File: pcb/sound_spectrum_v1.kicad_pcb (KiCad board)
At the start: 4 copper layers, 85.6 x 54 mm, 31 parts, among them J1 SWD_CONN, J2 Conn_02x10_Counter_Clockwise, P1 USB_C_Plug_USB2.0, SW2 SW_DPST_x2, U1 STM32G473CBTx, U2 AP2112K-3.3, U3 USBLC6-2SC6

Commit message: chore: further tracing
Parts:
- C12, C13, MK1-L1, MK1-R1: moved to B.Cu
- moved MK1-R1 60.6 mm to (125.8, 116.1), turned to 180 degrees
- moved J1 49.3 mm to (135.5, 72.7), turned to -90 degrees
- moved C13 43.1 mm to (123.5, 113.0), turned to 180 degrees
- moved MK1-L1 42.3 mm to (193.5, 116.0), turned to 180 degrees
- moved C14 40.6 mm to (126.2, 74.0), turned to 90 degrees
- moved U3 38.8 mm to (159.1, 79.6), turned to 90 degrees
- moved C12 38.4 mm to (191.2, 112.8), turned to 180 degrees
- moved SW2 38.4 mm to (141.8, 72.8)
- moved R4 36.1 mm to (170.2, 74.5), turned to 90 degrees
- moved FB1 33.9 mm to (167.0, 88.0)
- moved U2 29.2 mm to (167.7, 82.1), turned to -90 degrees
- moved R3 27.4 mm to (162.5, 79.5), turned to -90 degrees
- moved R6 26.6 mm to (146.0, 95.0), turned to 90 degrees
- moved D2 23.0 mm to (167.5, 74.5), turned to -90 degrees
- moved R5 22.9 mm to (148.2, 95.0), turned to 90 degrees
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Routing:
- net +3.3V: track 0.00 -> 112.2 mm
- net SWO: track 0.00 -> 31.6 mm
- net SWCLK: track 0.00 -> 28.5 mm
- net SWDIO: track 0.00 -> 28.5 mm
- net NRST: track 0.00 -> 27.0 mm
- net VBUS: track 0.00 -> 26.6 mm
- net USB_DP: track 0.00 -> 13.4 mm
- net USB_DM: track 0.00 -> 9.27 mm
- net I2C_SDA: track 0.00 -> 8.96 mm, vias 0 -> 2
- net +5V: track 0.00 -> 5.08 mm
- net BOOT0: track 0.00 -> 3.94 mm
- net Net-(P1-CC): track 0.00 -> 3.94 mm
- net USB_DM_EXT: track 0.00 -> 3.63 mm, vias 0 -> 1
- net USB_DP_EXT: track 0.00 -> 3.01 mm
- net Net-(D2-A): track 0.00 -> 2.76 mm
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- added copper zone on In1.Cu, net GND
- added copper zone on In2.Cu, net GND

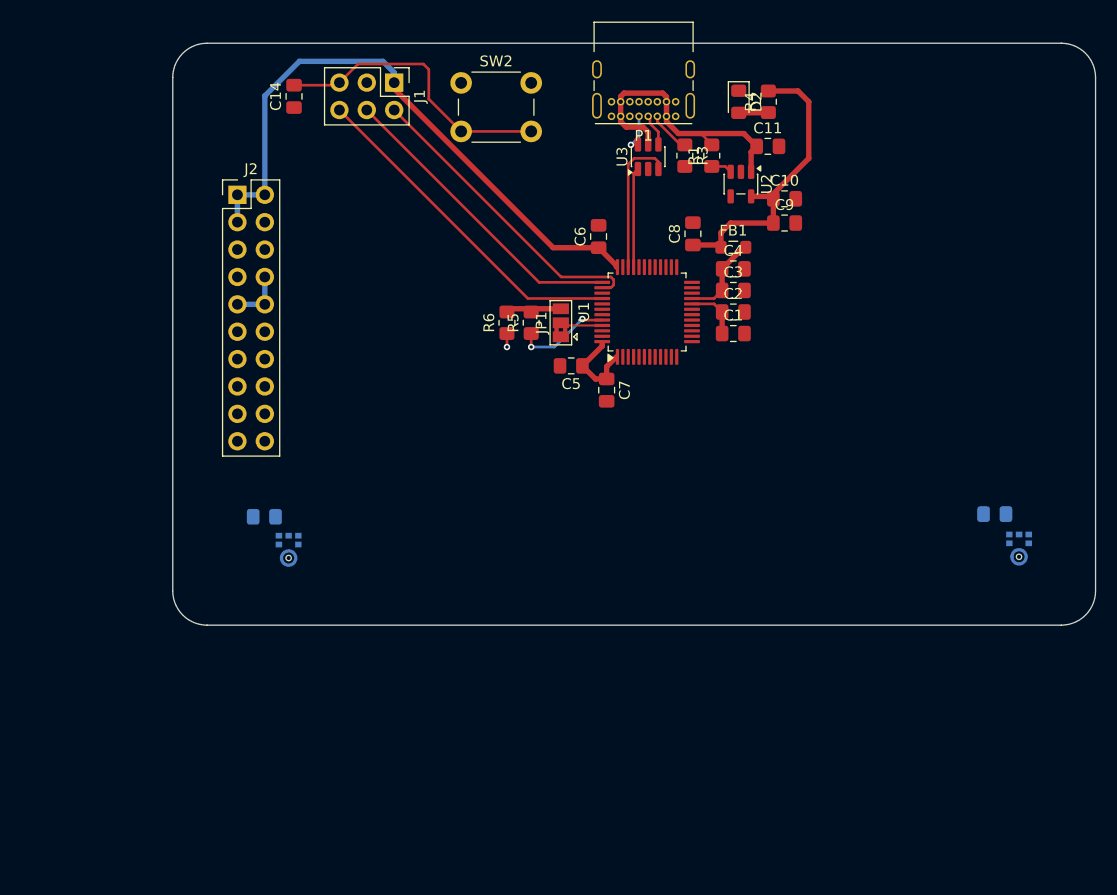
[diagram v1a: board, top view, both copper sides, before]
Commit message: fix: replace ics-43434 with ics-43432 due to part shortage
feat: make connections to all parts
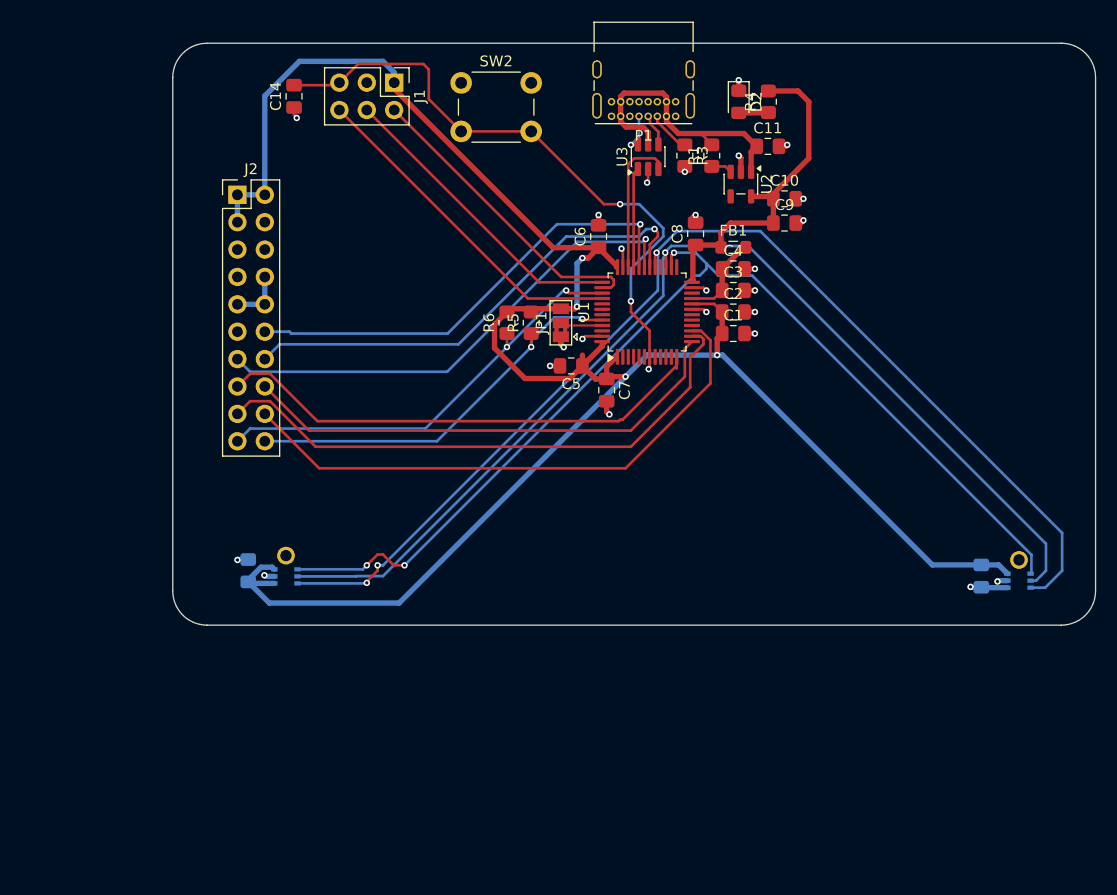
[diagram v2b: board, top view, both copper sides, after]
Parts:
- removed MK1-L1, MK1-R1: ICS-43434, Sensor_Audio:InvenSense_ICS-43434-6_3.5x2.65mm
- added IC1-L1: ICS-43432, Samacsys:ICS43432, B.Cu at (193.5, 117.0)
- added IC2-R1: ICS-43432, Samacsys:ICS43432, B.Cu at (125.5, 116.6)
- JP1: value Jumper_3_Bridged12 -> BOOT_SELECT
- moved C12 5.88 mm to (190.0, 118.5), turned to -90 degrees
- moved C13 5.22 mm to (122.0, 118.0), turned to 90 degrees
- moved C8 0.25 mm to (163.5, 86.8)
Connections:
- U1 pad 27: I2S_CLK -> I2S_CK
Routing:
- net +3.3V: track 112.2 -> 237.3 mm, vias 0 -> 4
- net I2S_SD: track 0.00 -> 107.2 mm, vias 0 -> 3
- net I2S_CK: track 0.00 -> 101.5 mm, vias 0 -> 1
- net I2S_WS: track 0.00 -> 98.8 mm, vias 0 -> 3
- net SPI_MISO: track 0.00 -> 52.8 mm
- net SPI_MOSI: track 0.00 -> 52.8 mm
- net SPI_NSS: track 0.00 -> 47.1 mm
- net SPI_SCK: track 0.00 -> 46.2 mm
- net UART_TX: track 0.00 -> 46.1 mm, vias 0 -> 1
- net UART_CK: track 0.00 -> 45.1 mm, vias 0 -> 1
- net UART_RX: track 0.00 -> 43.1 mm, vias 0 -> 1
- net I2C_SCL: track 1.25 -> 41.0 mm, vias 1 -> 2
- net NRST: track 27.0 -> 58.0 mm, vias 0 -> 3
- net GND: track 0.00 -> 29.7 mm, vias 0 -> 25
- net I2C_SDA: track 8.96 -> 37.8 mm

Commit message: chore: move traces around
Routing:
- net +3.3V: track 237.3 -> 228.0 mm, vias 4 -> 3
- net I2S_WS: track 98.8 -> 102.6 mm
- net I2S_CK: track 101.5 -> 105.3 mm
- net I2S_SD: track 107.2 -> 110.6 mm
- net SPI_NSS: track 47.1 -> 46.0 mm
- net GND: track 29.7 -> 30.7 mm, vias 25 -> 35

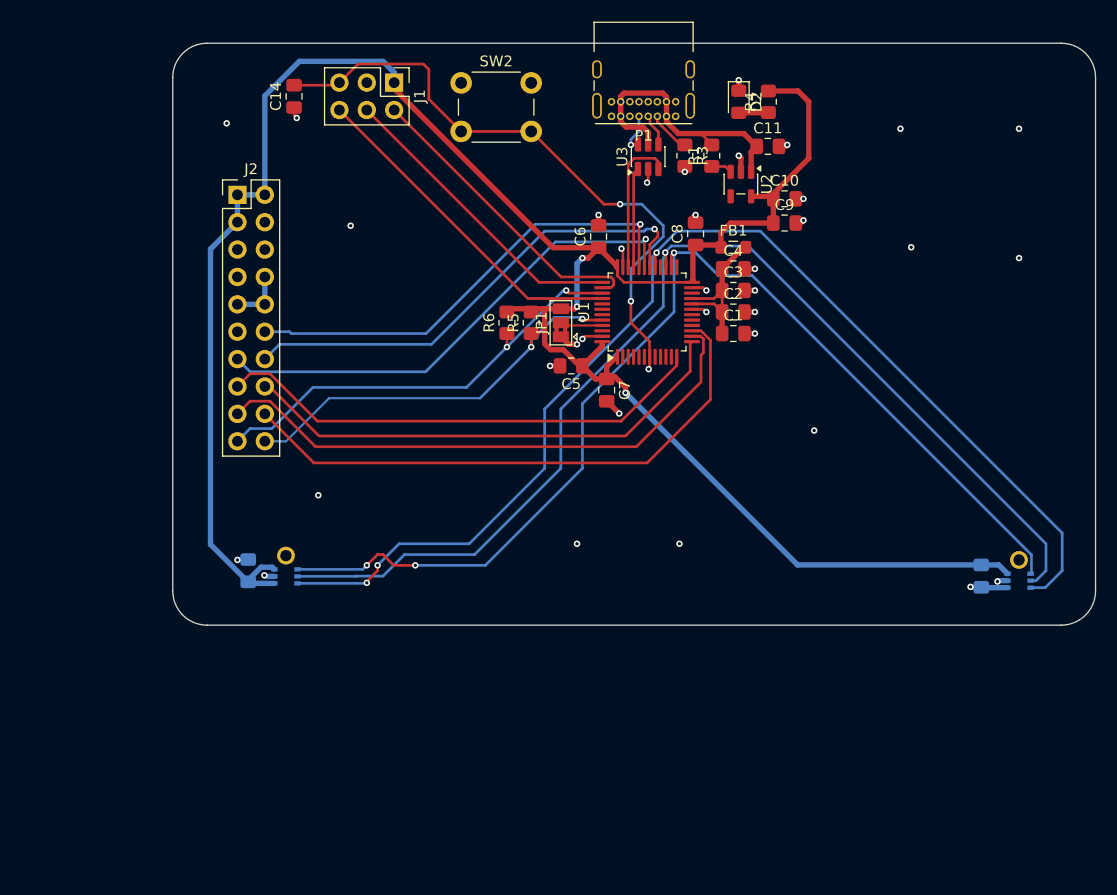
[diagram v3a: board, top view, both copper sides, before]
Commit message: feat: add HSE clock
feat: update schematic

chore: create gerber files
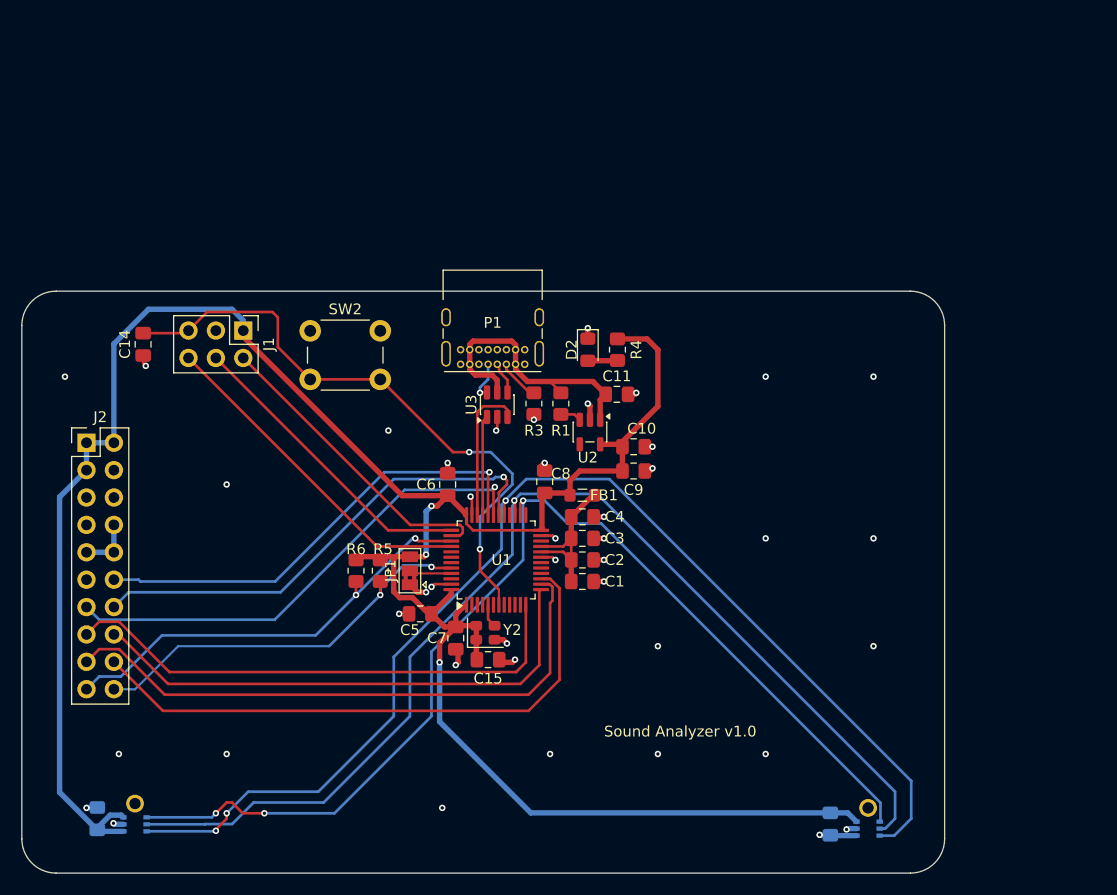
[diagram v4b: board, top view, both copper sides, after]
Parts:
- added C15: 100nF, Capacitor_SMD:C_0805_2012Metric_Pad1.18x1.45mm_HandSolder, F.Cu at (144.2, 126.2)
- added Y2: SG-210STF 48.0000ML5, Oscillator:Oscillator_SMD_SeikoEpson_SG210-4Pin_2.5x2.0mm, F.Cu at (144.0, 123.8)
- moved C1 26.9 mm to (153.0, 119.0)
- moved C10 26.9 mm to (157.8, 106.5)
- moved C11 26.9 mm to (156.2, 101.6)
- moved C12 26.9 mm to (176.0, 141.5)
- moved C13 26.9 mm to (108.0, 141.0)
- moved C14 26.9 mm to (112.2, 97.0)
- moved C2 26.9 mm to (153.0, 117.0)
- moved C3 26.9 mm to (153.0, 115.0)
- moved C4 26.9 mm to (153.0, 113.0)
- moved C5 26.9 mm to (138.0, 122.0)
- moved C6 26.9 mm to (140.5, 110.0)
- moved C7 26.9 mm to (141.2, 124.2)
- moved C8 26.9 mm to (149.5, 109.8)
- moved C9 26.9 mm to (157.8, 108.8)
- moved D2 26.9 mm to (153.5, 97.5)
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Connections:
- U1 pad 5: unconnected-(U1-PF0-Pad5) -> Net-(U1-PF0)
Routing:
- net +3.3V: track 228.0 -> 240.5 mm
- net SPI_NSS: track 46.0 -> 48.9 mm
- net GND: track 30.7 -> 33.6 mm, vias 35 -> 42
- net SPI_SCK: track 46.7 -> 49.2 mm
- net SPI_MISO: track 53.0 -> 55.3 mm
- net Net-(U1-PF0): track 0.00 -> 2.19 mm
- net SPI_MOSI: track 53.2 -> 55.0 mm
- net NRST: track 58.2 -> 57.0 mm, vias 3 -> 2
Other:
- board text added: "Sound Analyzer v1.0"

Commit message: chore: generated cpl file
fix: errors in schematic
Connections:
- J2 pad 10: +5V -> VBUS
- J2 pad 8: +5V -> VBUS
- J2 pad 9: +5V -> VBUS
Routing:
- net USB_DP: track 13.4 -> 0.00 mm
- net USB_DM: track 9.27 -> 0.00 mm
- net VBUS: track 26.6 -> 31.7 mm
- net +5V: track 5.08 -> 0.00 mm
